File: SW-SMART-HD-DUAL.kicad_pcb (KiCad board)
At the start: 2 copper layers, 76 x 76 mm, 52 parts, among them J1 SWD, J2 USART1, J3 PWRIN, SW1 BTS50010-1TAD, SW2 BTS50010-1TAD, U1 STM32G0B1KBTx, U3 LMR54410, U4 MCP2562

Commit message: lots of updates
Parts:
- CAN1: footprint TerminalBlock_TE-Connectivity:TerminalBlock_TE_282834-3_1x03_P2.54mm_Horizontal -> TerminalBlock_Phoenix:TerminalBlock_Phoenix_MPT-0,5-3-2.54_1x03_P2.54mm_Horizontal
- J3: footprint TerminalBlock_Phoenix:TerminalBlock_Phoenix_MKDS-3-2-5.08_1x02_P5.08mm_Horizontal -> TerminalBlock_Phoenix:TerminalBlock_Phoenix_MPT-0,5-2-2.54_1x02_P2.54mm_Horizontal
- moved C3V0 7.79 mm to (125.8, 83.7)
- moved C5V2 7.79 mm to (115.2, 83.8)
- moved C5V3 7.79 mm to (110.4, 83.8)
- moved CAN1 7.79 mm to (130.4, 49.8)
- moved CB1 7.79 mm to (107.4, 88.9)
- moved CDIV1 7.79 mm to (111.2, 77.2)
- moved CIN2 7.79 mm to (100.5, 38.7)
- moved CIS1 7.79 mm to (116.5, 39.1)
- moved CIS2 7.79 mm to (115.0, 39.1)
- moved CMCP1 7.79 mm to (134.0, 56.8)
- moved CNRST1 7.79 mm to (118.3, 71.7)
- moved COUT1 7.79 mm to (89.3, 79.2)
- moved COUT2 7.79 mm to (88.3, 40.2)
- moved CS1 7.79 mm to (108.2, 62.1)
- moved CSTM1 7.79 mm to (116.5, 67.7)
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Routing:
- net GND: track 4.71 -> 9.36 mm, vias 2 -> 0
- net /VS: track 19.2 -> 20.4 mm
- net +12V: track 8.86 -> 9.96 mm, vias 545 -> 546
- net /SW1IS_PD: track 6.01 -> 6.60 mm

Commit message: layout complete, drc passed
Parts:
- moved CIS1 46.5 mm to (97.0, 81.2), turned to 90 degrees
- moved CIS2 14.6 mm to (100.5, 38.7)
- moved RVDIV1 8.24 mm to (115.2, 76.2)
- moved CDIV1 4.51 mm to (115.2, 79.2), turned to 180 degrees
- moved RVDIV2 4.10 mm to (115.2, 77.8), turned to 0 degrees
- moved CIN2 1.50 mm to (102.0, 38.7)
- moved RIN2 1.50 mm to (103.5, 38.7)
- moved RIS1 1.50 mm to (100.0, 81.2)
- moved RIS_PROT1 1.50 mm to (98.5, 81.2)
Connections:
- U1 pad 7: /SW1IS -> /SW2IS
- U1 pad 8: unconnected-(U1-PA1-Pad8) -> /SW1IS
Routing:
- net /SW2IS: track 0.00 -> 58.3 mm, vias 0 -> 2
- net /SW2IN: track 0.00 -> 41.6 mm, vias 0 -> 2
- net /SW1IN: track 0.00 -> 39.4 mm, vias 0 -> 2
- net +5V: track 46.9 -> 70.2 mm, vias 1 -> 2
- net /SW1IS: track 12.9 -> 30.5 mm, vias 1 -> 2
- net /SWCLK: track 16.0 -> 29.2 mm, vias 2 -> 1
- net /CAN_L: track 2.12 -> 13.9 mm, vias 0 -> 1
- net /NRST: track 5.37 -> 15.3 mm, vias 0 -> 1
- net /VS: track 20.4 -> 10.7 mm, vias 2 -> 0
- net /CAN_H: track 2.89 -> 11.0 mm
- net +3.3V: track 59.2 -> 65.2 mm
- net GND: track 9.36 -> 13.5 mm
- net Net-(SW2-IN): track 5.79 -> 7.42 mm
- net /SW1IS_PD: track 6.60 -> 7.92 mm
- net +12V: track 9.96 -> 10.4 mm, vias 546 -> 549
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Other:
- board text added: "3V3 TXD RXD GND"
- board text added: "RST 3V3 CLK DIO GND"
- board text removed: "1"
- board text removed: "POWER IN"

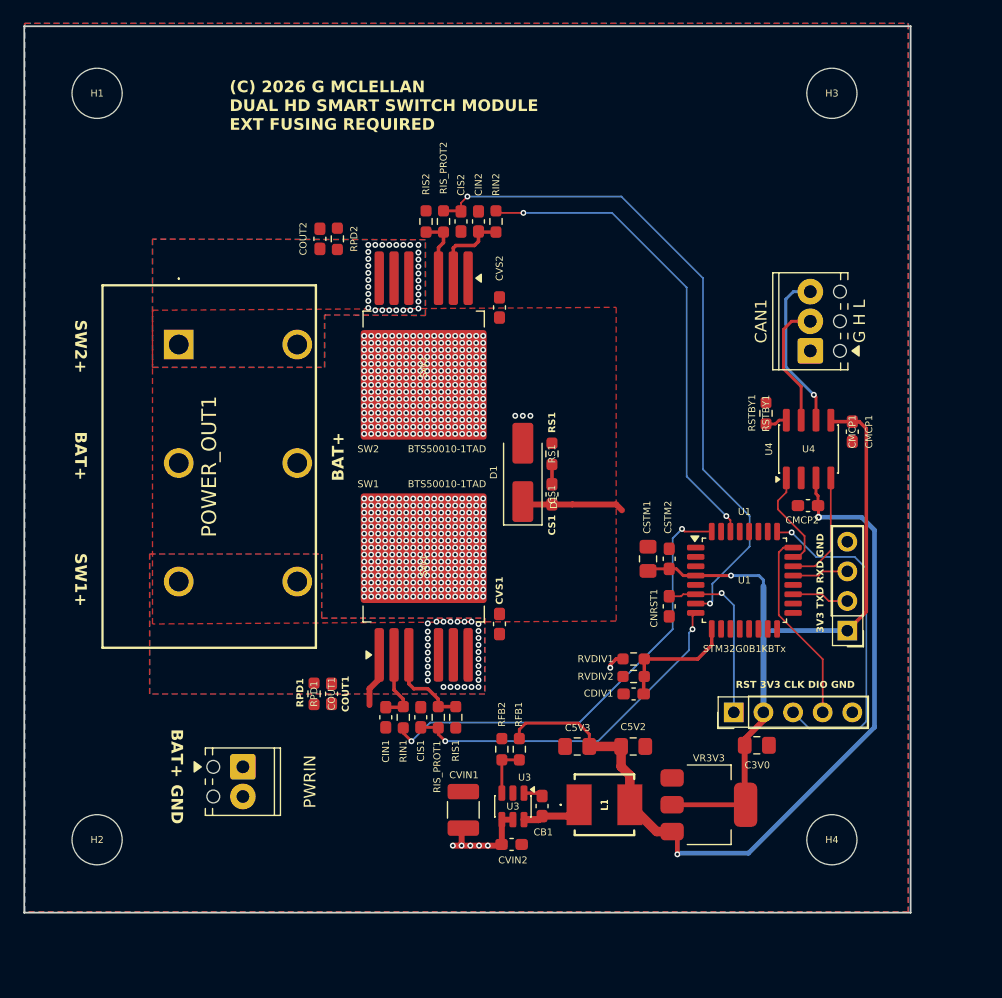
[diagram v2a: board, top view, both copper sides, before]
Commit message: added crystal osc, fixed some silkscreen issues, moved a few tracks
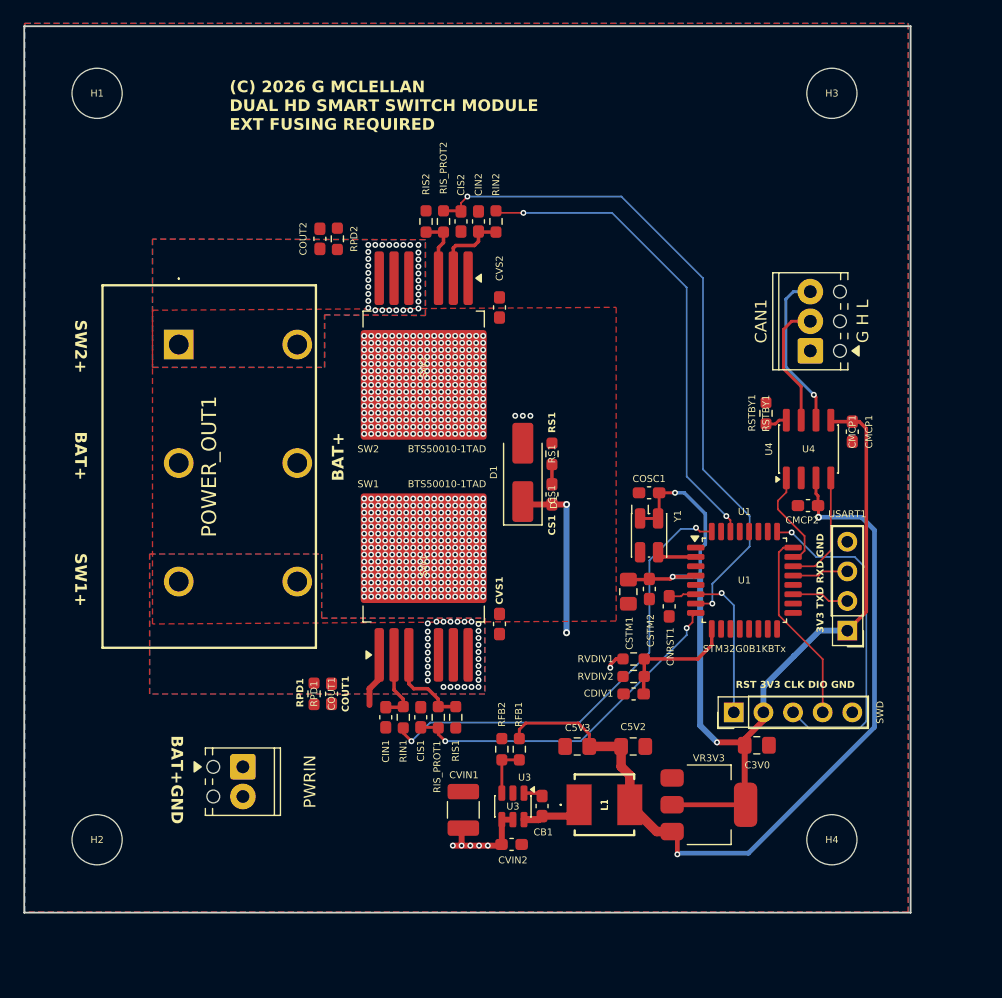
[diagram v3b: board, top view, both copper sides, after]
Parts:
- added COSC1: 100n, Capacitor_SMD:C_0603_1608Metric_Pad1.08x0.95mm_HandSolder, F.Cu at (116.6, 62.0)
- added Y1: 8MHz, Oscillator:Oscillator_SMD_EuroQuartz_XO32-4Pin_3.2x2.5mm_RotB_HandSoldering, F.Cu at (116.6, 65.7)
- moved CSTM1 3.28 mm to (114.8, 70.5), turned to -90 degrees
- moved CSTM2 3.10 mm to (116.6, 70.2), turned to -90 degrees
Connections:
- U1 pad 2: unconnected-(U1-PC14-Pad2) -> /OSC
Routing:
- net +3.3V: track 65.2 -> 87.3 mm, vias 1 -> 3
- net GND: track 13.5 -> 19.5 mm, vias 0 -> 2
- net /OSC: track 0.00 -> 3.39 mm
- net /SW1IS: track 30.5 -> 29.6 mm
